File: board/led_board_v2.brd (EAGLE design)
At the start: 50.3 x 47.4 mm, 22 parts

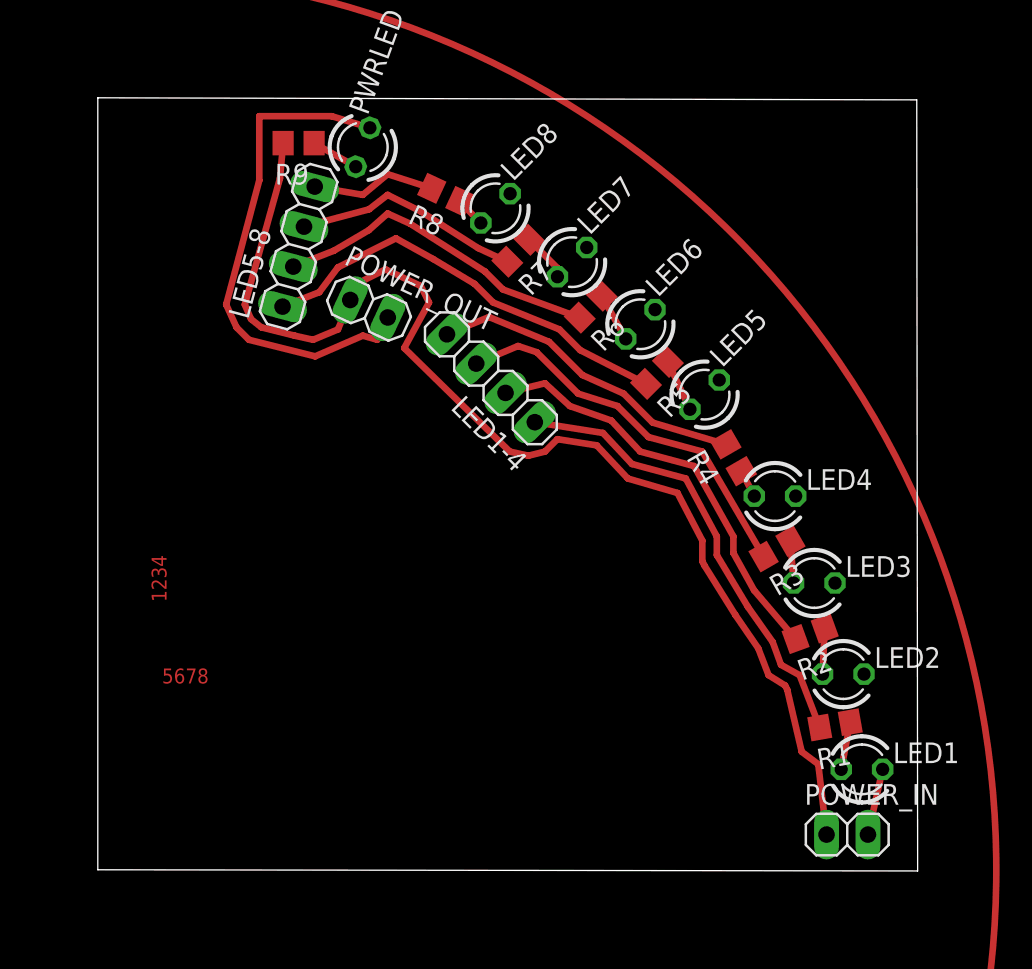
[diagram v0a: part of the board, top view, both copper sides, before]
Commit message: fixed led board layout v2
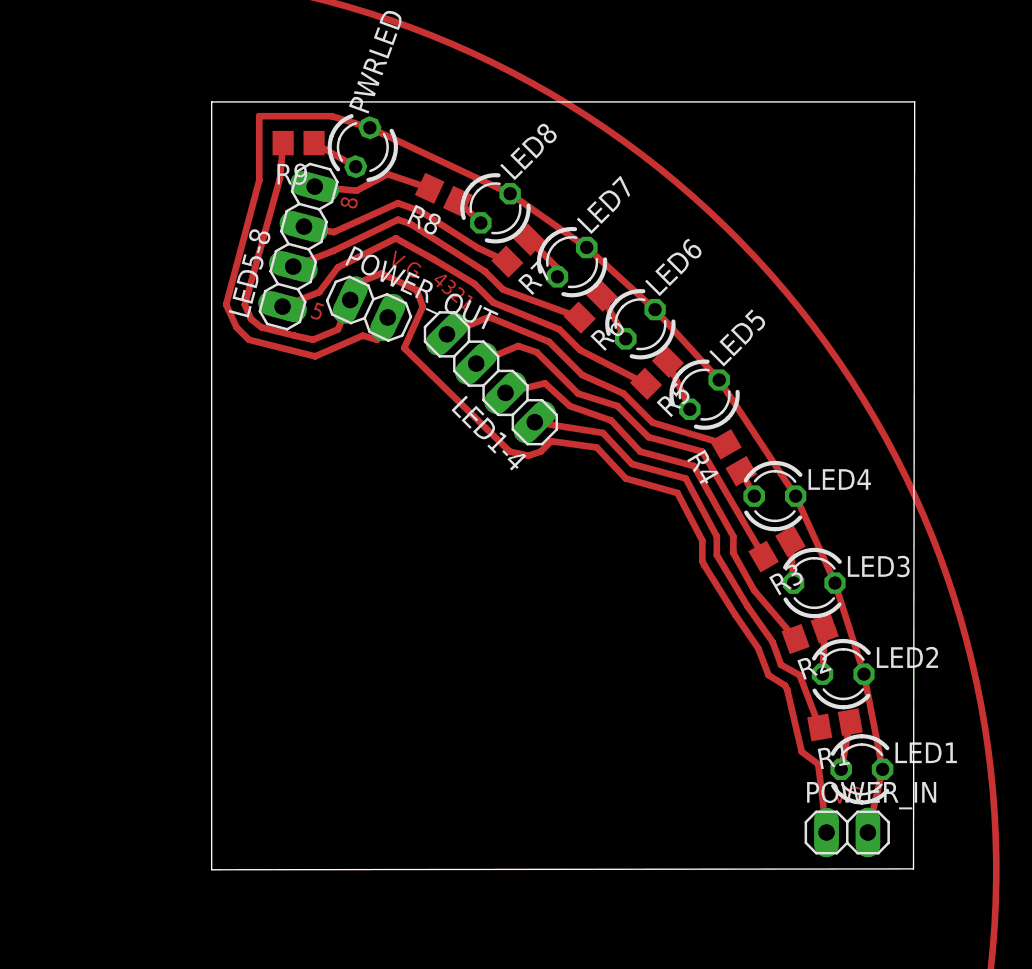
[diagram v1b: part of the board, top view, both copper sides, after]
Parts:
- moved R8 0.13 mm to (21.2, 41.4)
- moved POWER_IN 0.13 mm to (46.0, 2.29)
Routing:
- net GND: track 35.2 -> 88.1 mm
- net +5V: track 73.0 -> 72.0 mm
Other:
- board size 50.3 x 47.4 mm -> 43.1 x 47.1 mm
- board text added: "4321"
- board text added: "5"
- board text added: "8"
- board text added: "V G"
- board text added: "VG"
- board text removed: "1234"
- board text removed: "5678"
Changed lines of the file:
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@@
 <board>
 <plain>
-<wire x1="0" y1="0" x2="50.292" y2="-0.073" width="0" layer="20"/>
-<wire x1="50.292" y1="-0.073" x2="50.238" y2="47.229" width="0" layer="20"/>
-<wire x1="50.238" y1="47.229" x2="0" y2="47.356" width="0" layer="20"/>
-<wire x1="0" y1="47.356" x2="0" y2="0" width="0" layer="20"/>
-<text x="3.937" y="11.43" size="0.9144" layer="1" font="vector" ratio="28">5678</text>
-<text x="3.302" y="19.304" size="0.9144" layer="1" font="vector" ratio="28" rot="R270">1234</text>
+<wire x1="6.985" y1="0" x2="50.038" y2="0.054" width="0" layer="20"/>
+<wire x1="50.038" y1="0.054" x2="50.111" y2="47.102" width="0" layer="20"/>
+<wire x1="50.111" y1="47.102" x2="6.985" y2="47.102" width="0" layer="20"/>
+<wire x1="6.985" y1="47.102" x2="6.985" y2="0" width="0" layer="20"/>
+<text x="14.986" y="41.402" size="1.016" layer="1" font="vector" ratio="28" rot="R260">8</text>
+<text x="20.447" y="36.068" size="0.9144" layer="1" font="vector" ratio="28" rot="R320">4321</text>
 <circle x="0" y="0" radius="55.118" width="0.4064" layer="1"/>
+<text x="12.954" y="33.909" size="1.016" layer="1" font="vector" ratio="28" rot="R340">5</text>
+<text x="17.78" y="37.211" size="0.9144" layer="1" font="vector" ratio="28" rot="R330">V G</text>
+<text x="45.085" y="4.064" size="1.016" layer="1" font="vector" ratio="28">VG</text>
 </plain>
 <attributes>
@@
 <element name="R6" library="resistor" package="R0805" value="470" x="30.237" y="34.5445" rot="R225"/>
 <element name="R7" library="resistor" package="R0805" value="470" x="25.792" y="37.9735" rot="R225"/>
-<element name="R8" library="resistor" package="R0805" value="470" x="21.347" y="41.4025" rot="R155"/>
+<element name="R8" library="resistor" package="R0805" value="470" x="21.22" y="41.4025" rot="R155"/>
 <element name="LED1-4" library="pinhead" package="1X04" value="JP1" x="24.113" y="30.1515" rot="R135"/>
 <element name="POWER_OUT" library="pinhead" package="1X02" value="JP3" x="16.637" y="34.417" rot="R335"/>
-<element name="POWER_IN" library="pinhead" package="1X02" value="JP2" x="45.974" y="2.159"/>
+<element name="POWER_IN" library="pinhead" package="1X02" value="JP2" x="45.974" y="2.286"/>
 <element name="LED5-8" library="pinhead" package="1X04" value="JP2" x="12.319" y="38.227" rot="R75"/>
 <element name="R9" library="resistor" package="R0805" value="470" x="12.319" y="44.577" rot="R180"/>
@@
 <contactref element="POWER_IN" pad="2"/>
 <contactref element="POWER_OUT" pad="2"/>
-<wire x1="47.244" y1="2.159" x2="48.144" y2="6.16" width="0.4064" layer="1"/>
+<wire x1="47.244" y1="2.286" x2="48.144" y2="6.16" width="0.4064" layer="1"/>
 <contactref element="PWRLED" pad="K"/>
 <wire x1="17.788009375" y1="33.880271875" x2="17.145" y2="32.512" width="0.4064" layer="1"/>
@@
 <wire x1="9.906" y1="46.228" x2="14.351" y2="46.228" width="0.4064" layer="1"/>
 <wire x1="14.351" y1="46.228" x2="16.6903625" y2="45.516409375" width="0.4064" layer="1"/>
-<wire x1="34.183025" y1="34.363025" x2="38.120025" y2="30.045025" width="0" layer="19" extent="1-1"/>
-<wire x1="29.992025" y1="38.173025" x2="34.183025" y2="34.363025" width="0" layer="19" extent="1-1"/>
-<wire x1="25.293025" y1="41.475025" x2="29.992025" y2="38.173025" width="0" layer="19" extent="1-1"/>
-<wire x1="42.81" y1="22.924" x2="38.120025" y2="30.045025" width="0" layer="19" extent="1-1"/>
-<wire x1="45.223" y1="17.59" x2="42.81" y2="22.924" width="0" layer="19" extent="1-1"/>
-<wire x1="47.001" y1="12.002" x2="45.223" y2="17.59" width="0" layer="19" extent="1-1"/>
-<wire x1="48.144" y1="6.16" x2="47.001" y2="12.002" width="0" layer="19" extent="1-1"/>
-<wire x1="16.6903625" y1="45.516409375" x2="25.293025" y2="41.475025" width="0" layer="19" extent="1-1"/>
+<wire x1="16.6903625" y1="45.516409375" x2="25.293025" y2="41.475025" width="0.4064" layer="1"/>
+<wire x1="25.293025" y1="41.475025" x2="29.992025" y2="38.173025" width="0.4064" layer="1"/>
+<wire x1="29.992025" y1="38.173025" x2="34.183025" y2="34.363025" width="0.4064" layer="1"/>
+<wire x1="34.183025" y1="34.363025" x2="38.120025" y2="30.045025" width="0.4064" layer="1"/>
+<wire x1="38.120025" y1="30.045025" x2="42.81" y2="22.924" width="0.4064" layer="1"/>
+<wire x1="42.81" y1="22.924" x2="45.223" y2="17.59" width="0.4064" layer="1"/>
+<wire x1="45.223" y1="17.59" x2="47.001" y2="12.002" width="0.4064" layer="1"/>
+<wire x1="47.001" y1="12.002" x2="48.144" y2="6.16" width="0.4064" layer="1"/>
 </signal>
 <signal name="N$5">
@@
 <contactref element="R8" pad="1"/>
 <contactref element="LED8" pad="A"/>
-<wire x1="22.207990625" y1="41.0010125" x2="23.080196875" y2="40.095746875" width="0.4064" layer="1"/>
+<wire x1="22.080990625" y1="41.0010125" x2="23.080196875" y2="40.095746875" width="0.4064" layer="1"/>
 <wire x1="23.080196875" y1="40.095746875" x2="23.496971875" y2="39.678971875" width="0.4064" layer="1"/>
 </signal>
@@
 <wire x1="24.85475" y1="35.59725" x2="29.565246875" y2="33.872746875" width="0.4064" layer="1"/>
 <wire x1="11.990296875" y1="37.000271875" x2="14.478" y2="37.973" width="0.4064" layer="1"/>
-<wire x1="14.478" y1="37.973" x2="16.637" y2="39.243" width="0.4064" layer="1"/>
-<wire x1="16.637" y1="39.243" x2="17.78" y2="40.259" width="0.4064" layer="1"/>
-<wire x1="17.78" y1="40.259" x2="19.177" y2="39.624" width="0.4064" layer="1"/>
+<wire x1="14.478" y1="37.973" x2="18.415" y2="39.878" width="0.4064" layer="1"/>
+<wire x1="18.415" y1="39.878" x2="19.177" y2="39.624" width="0.4064" layer="1"/>
 </signal>
 <signal name="LED7">
@@
 <wire x1="19.812" y1="40.386" x2="23.33075" y2="38.13725" width="0.4064" layer="1"/>
 <wire x1="23.33075" y1="38.13725" x2="25.120246875" y2="37.301746875" width="0.4064" layer="1"/>
-<wire x1="12.6477" y1="39.453725" x2="16.637" y2="40.513" width="0.4064" layer="1"/>
-<wire x1="16.637" y1="40.513" x2="17.78" y2="41.402" width="0.4064" layer="1"/>
-<wire x1="17.78" y1="41.402" x2="19.812" y2="40.386" width="0.4064" layer="1"/>
+<wire x1="12.6477" y1="39.453725" x2="14.478" y2="39.116" width="0.4064" layer="1"/>
+<wire x1="14.478" y1="39.116" x2="18.415" y2="40.894" width="0.4064" layer="1"/>
+<wire x1="18.415" y1="40.894" x2="19.812" y2="40.386" width="0.4064" layer="1"/>
 </signal>
 <signal name="LED8">
 <contactref element="R8" pad="2"/>
 <contactref element="LED5-8" pad="4"/>
-<wire x1="20.48600625" y1="41.803984375" x2="17.78" y2="42.672" width="0.4064" layer="1"/>
-<wire x1="17.78" y1="42.672" x2="16.256" y2="41.402" width="0.4064" layer="1"/>
-<wire x1="16.256" y1="41.402" x2="13.3051" y2="41.907175" width="0.4064" layer="1"/>
+<wire x1="20.35900625" y1="41.803984375" x2="17.78" y2="42.672" width="0.4064" layer="1"/>
+<wire x1="17.78" y1="42.672" x2="15.875" y2="41.656" width="0.4064" layer="1"/>
+<wire x1="15.875" y1="41.656" x2="13.3051" y2="41.907175" width="0.4064" layer="1"/>
 </signal>
 <signal name="LED1">
@@
 <contactref element="POWER_IN" pad="1"/>
 <contactref element="POWER_OUT" pad="1"/>
-<wire x1="44.704" y1="2.159" x2="44.196" y2="6.477" width="0.4064" layer="1"/>
+<wire x1="44.704" y1="2.286" x2="44.196" y2="6.477" width="0.4064" layer="1"/>
 <wire x1="44.196" y1="6.477" x2="43.18" y2="7.239" width="0.4064" layer="1"/>
 <wire x1="43.18" y1="7.239" x2="42.291" y2="11.049" width="0.4064" layer="1"/>
@@
 <wire x1="37.084" y1="18.923" x2="37.084" y2="20.193" width="0.4064" layer="1"/>
 <wire x1="37.084" y1="20.193" x2="35.56" y2="23.114" width="0.4064" layer="1"/>
-<wire x1="35.56" y1="23.114" x2="32.512" y2="24.003" width="0.4064" layer="1"/>
-<wire x1="32.512" y1="24.003" x2="30.607" y2="26.035" width="0.4064" layer="1"/>
-<wire x1="30.607" y1="26.035" x2="28.194" y2="26.416" width="0.4064" layer="1"/>
-<wire x1="28.194" y1="26.416" x2="27.432" y2="25.654" width="0.4064" layer="1"/>
-<wire x1="27.432" y1="25.654" x2="26.416" y2="25.4" width="0.4064" layer="1"/>
+<wire x1="35.56" y1="23.114" x2="32.385" y2="24.003" width="0.4064" layer="1"/>
+<wire x1="32.385" y1="24.003" x2="30.607" y2="25.908" width="0.4064" layer="1"/>
+<wire x1="30.607" y1="25.908" x2="27.813" y2="26.289" width="0.4064" layer="1"/>
+<wire x1="27.813" y1="26.289" x2="27.178" y2="25.654" width="0.4064" layer="1"/>
+<wire x1="27.178" y1="25.654" x2="26.416" y2="25.4" width="0.4064" layer="1"/>
 <wire x1="26.416" y1="25.4" x2="25.273" y2="25.654" width="0.4064" layer="1"/>
 <wire x1="25.273" y1="25.654" x2="18.796" y2="32.004" width="0.4064" layer="1"/>
 <contactref element="R9" pad="2"/>
-<wire x1="18.796" y1="32.004" x2="20.32" y2="34.798" width="0.4064" layer="1"/>
-<wire x1="20.32" y1="34.798" x2="19.812" y2="35.814" width="0.4064" layer="1"/>
-<wire x1="19.812" y1="35.814" x2="17.653" y2="36.83" width="0.4064" layer="1"/>
-<wire x1="17.653" y1="36.83" x2="16.129" y2="36.068" width="0.4064" layer="1"/>
+<wire x1="18.796" y1="32.004" x2="19.939" y2="34.544" width="0.4064" layer="1"/>
+<wire x1="19.939" y1="34.544" x2="19.558" y2="35.56" width="0.4064" layer="1"/>
+<wire x1="19.558" y1="35.56" x2="17.399" y2="36.576" width="0.4064" layer="1"/>
+<wire x1="17.399" y1="36.576" x2="16.129" y2="36.068" width="0.4064" layer="1"/>
 <wire x1="16.129" y1="36.068" x2="15.4859875" y2="34.953725" width="0.4064" layer="1"/>
 <wire x1="11.369" y1="44.577" x2="11.176" y2="42.418" width="0.4064" layer="1"/>

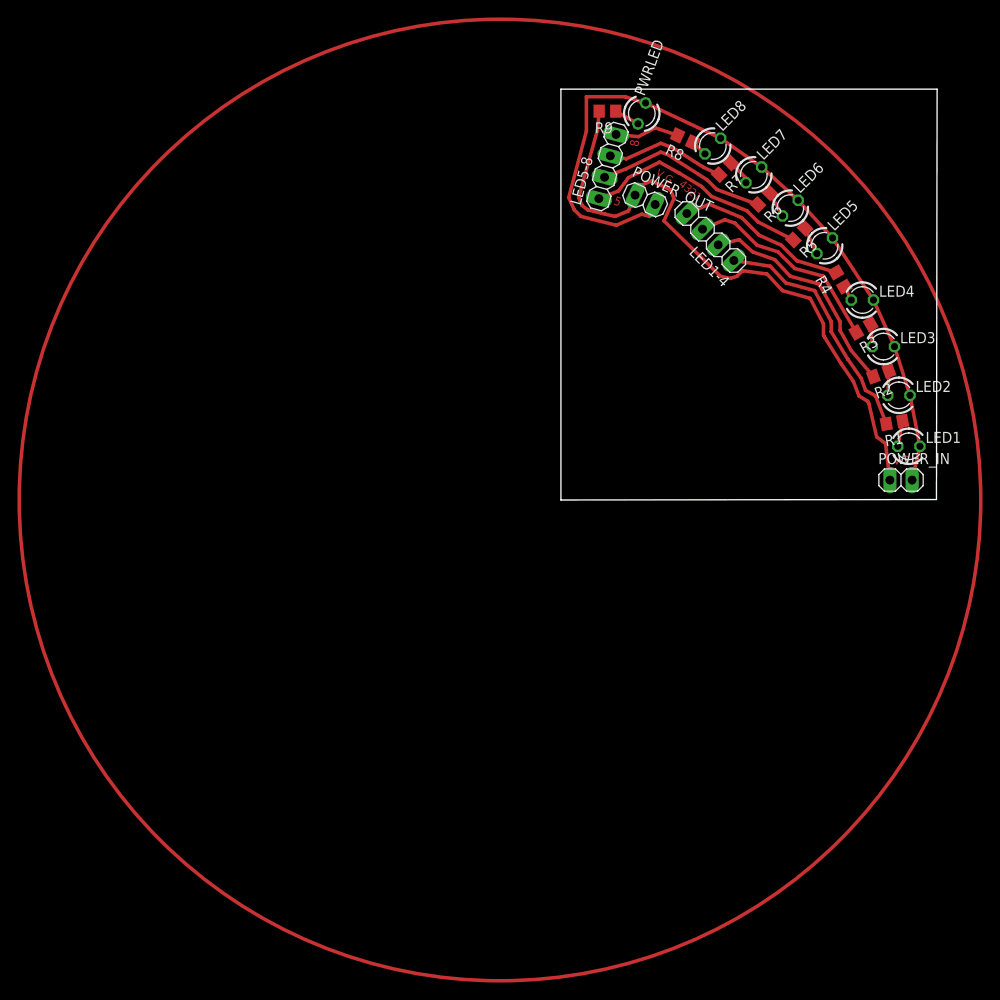
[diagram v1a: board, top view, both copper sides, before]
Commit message: started to swap layer to bottom. not done!
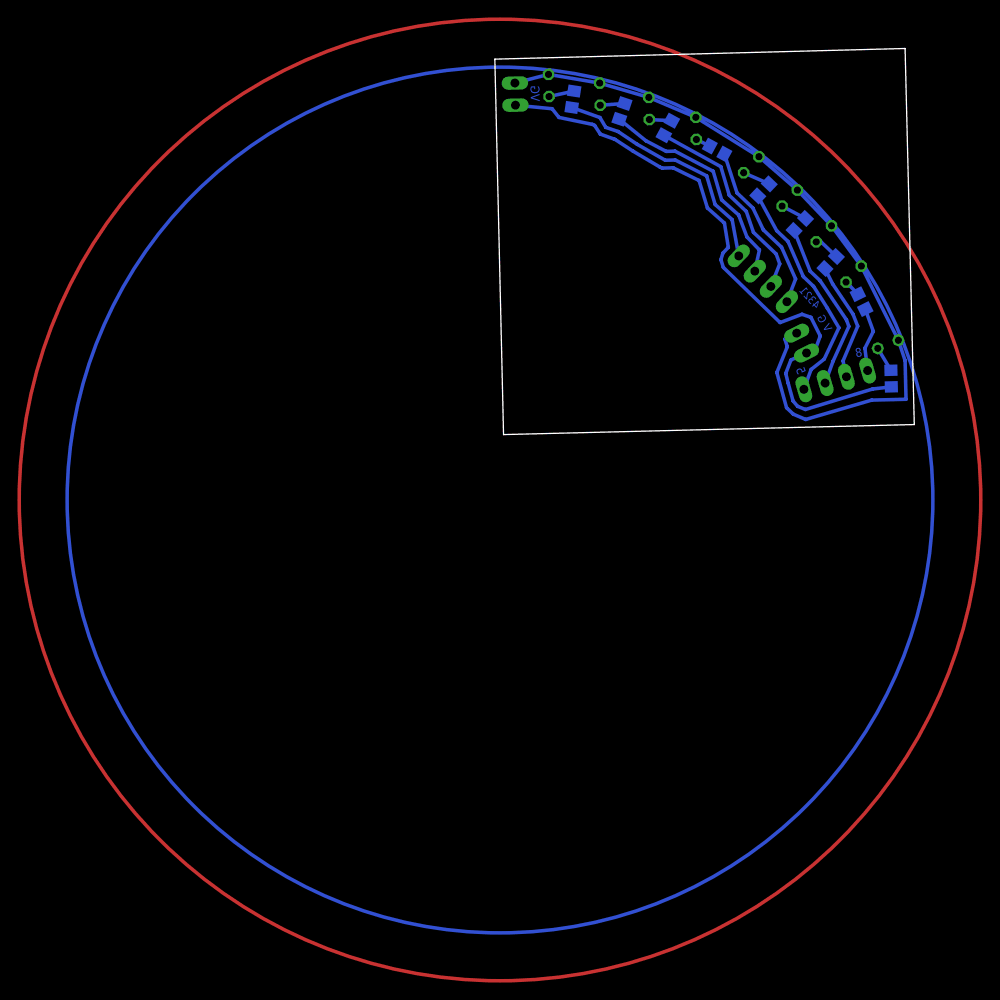
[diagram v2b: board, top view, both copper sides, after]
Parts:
- moved POWER_IN 62.6 mm to (1.74, 46.5), flipped to the bottom, turned to 88.6 degrees
- moved LED1 58.4 mm to (5.59, 47.5), flipped to the bottom, turned to 88.6 degrees
- moved R1 52.3 mm to (8.36, 45.9), flipped to the bottom, turned to 278.6 degrees
- moved LED2 48.6 mm to (11.5, 46.5), flipped to the bottom, turned to 88.6 degrees
- moved R9 44.7 mm to (44.8, 13.9), flipped to the bottom, turned to 268.6 degrees
- moved R2 42.3 mm to (14.0, 44.6), flipped to the bottom, turned to 288.6 degrees
- moved PWRLED 38.7 mm to (44.5, 17.8), flipped to the bottom, turned to 158.6 degrees
- moved LED3 38.3 mm to (17.1, 44.9), flipped to the bottom, turned to 88.6 degrees
- moved LED5-8 35.8 mm to (38.5, 13.8), flipped to the bottom, turned to 163.6 degrees
- moved R3 32.1 mm to (19.2, 42.7), flipped to the bottom, turned to 298.6 degrees
- moved R8 27.5 mm to (41.4, 22.7), flipped to the bottom, turned to 243.6 degrees
- moved LED4 27.4 mm to (22.5, 42.6), flipped to the bottom, turned to 88.6 degrees
- moved POWER_OUT 24.3 mm to (34.6, 18.0), flipped to the bottom, turned to 63.6 degrees
- moved LED8 21.8 mm to (40.5, 25.9), flipped to the bottom, turned to 133.6 degrees
- moved R4 20.5 mm to (24.9, 40.1), flipped to the bottom, turned to 208.6 degrees
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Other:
- board size 43.1 x 47.1 mm -> 48.1 x 44.3 mm
